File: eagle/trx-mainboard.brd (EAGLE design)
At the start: 95.3 x 82.5 mm, 38 parts, among them J1 629722000214, J2 DF12NB(3.0)-10DP-0.5V, P1 S2B-PH-SM4-TB, Q1 BSS84, U2 BQ2407X

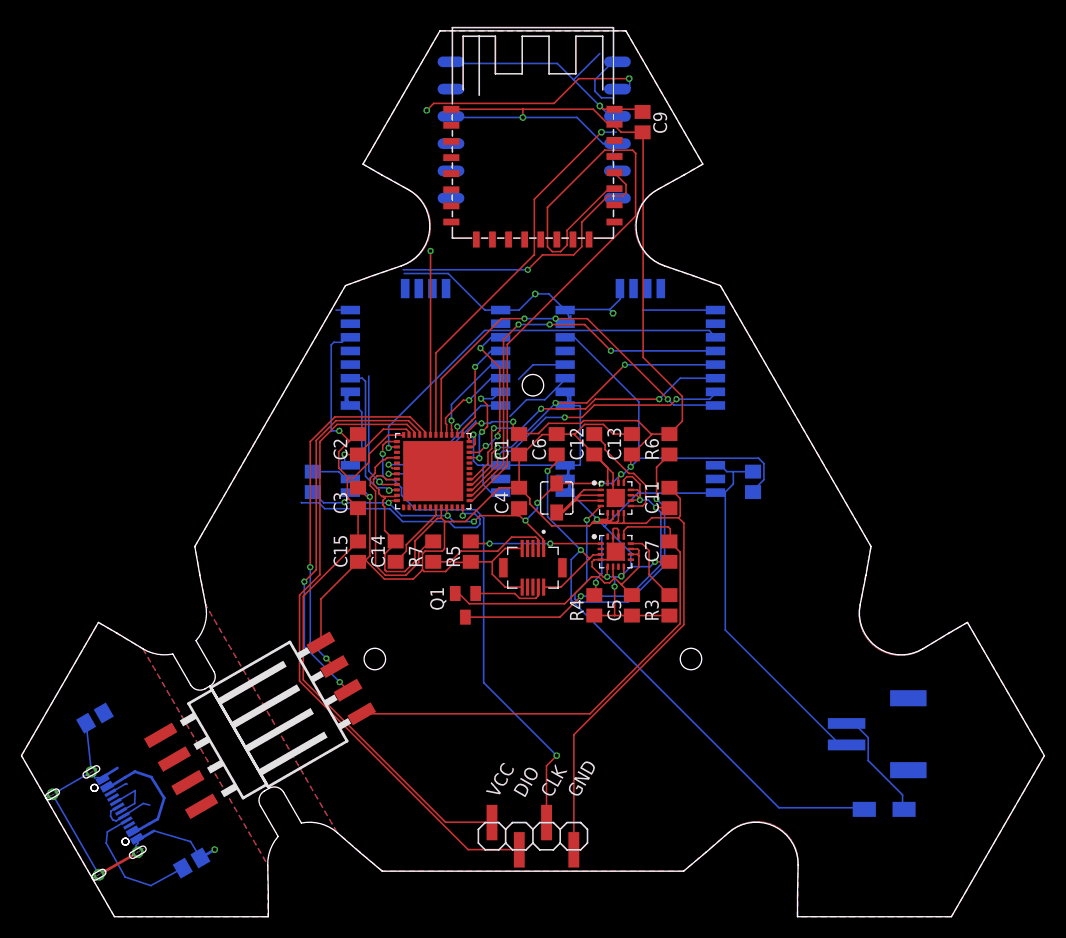
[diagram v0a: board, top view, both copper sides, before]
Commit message: Designed new boards wit fixed errors
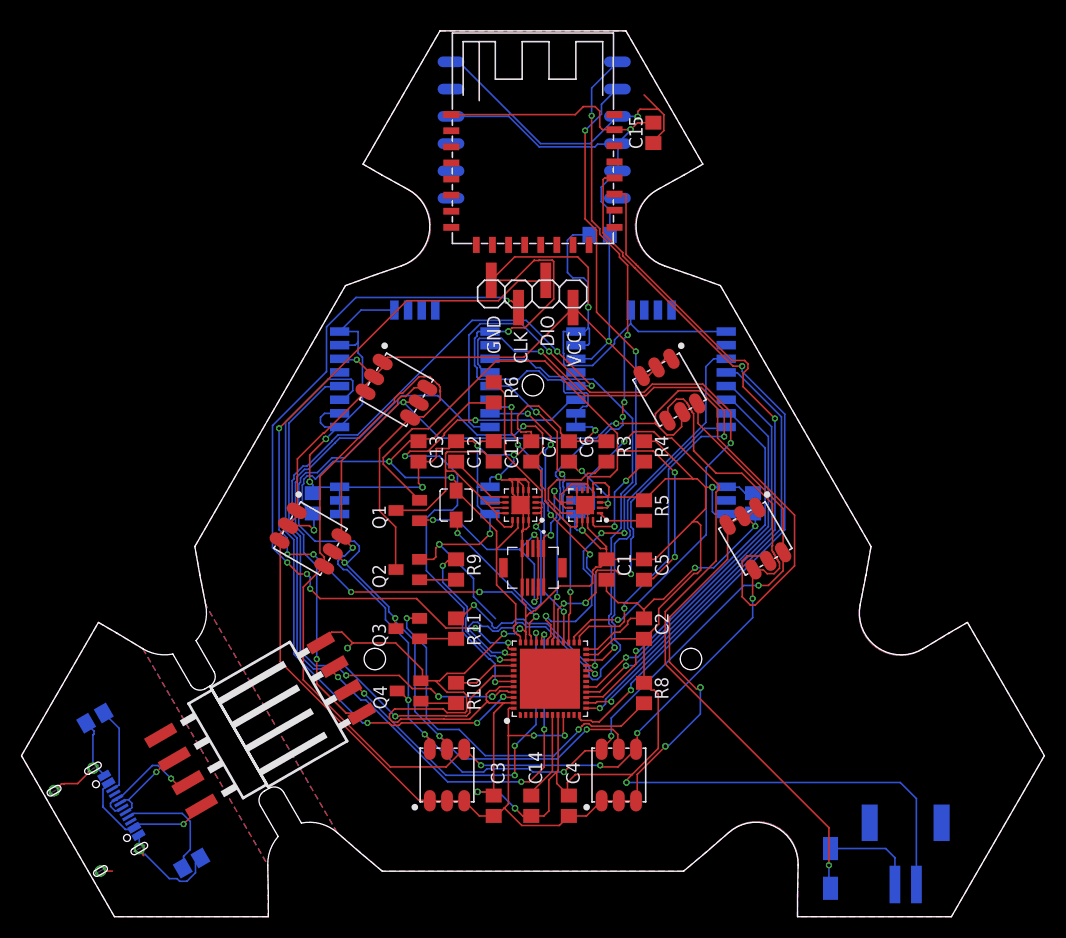
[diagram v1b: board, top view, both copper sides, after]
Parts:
- removed R7: 33R, rcl:R0805
- added Q2, Q3, Q4: BSS123, transistor-small-signal:SOT23
- added R10, R11, R8, R9: (no value), rcl:R0805
- added U$12, U$13, U$6, U$7, U$8, U$9: RGB_LED, led:PLCC6
- moved JP1 50.7 mm to (51.3, 59.0), turned to 180 degrees
- moved C15 47.7 mm to (60.0, 74.0)
- moved C2 31.7 mm to (59.1, 27.8)
- moved C3 31.3 mm to (45.1, 11.3)
- moved C4 29.0 mm to (52.1, 11.3)
- moved C14 26.8 mm to (48.6, 11.3), turned to 90 degrees
- moved U$10 22.2 mm to (50.4, 23.2)
- moved C13 19.9 mm to (38.1, 44.3), turned to 270 degrees
- moved R6 17.1 mm to (45.1, 49.8), turned to 90 degrees
- moved C11 16.9 mm to (45.1, 44.3)
- moved R5 16.6 mm to (59.1, 38.8), turned to 90 degrees
- moved C7 15.9 mm to (48.6, 44.3), turned to 90 degrees
- moved R3 15.5 mm to (55.6, 44.3), turned to 270 degrees
- moved R4 15.1 mm to (59.1, 44.3), turned to 270 degrees
- moved P1 15.0 mm to (83.5, 4.00), turned to 0 degrees
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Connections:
- removed net LED_D: J2.3, R7.1
- removed net N$10: R7.2, U$10.40
- removed net N$9: C5.1, Q1.2, U2.10, U2.11, U2.6
- new net CAT_B: Q4.3, U$12.2, U$13.2, U$6.2, U$7.2, U$8.2, U$9.2
- new net CAT_G: Q2.3, U$12.6, U$13.6, U$6.6, U$7.6, U$8.6, U$9.6
- new net CAT_R: Q3.3, U$12.4, U$13.4, U$6.4, U$7.4, U$8.4, U$9.4
- new net LED_B: R10.2, U$10.40
- new net LED_G: R9.2, U$10.39
- new net LED_R: R11.2, U$10.20
- new net N$13: Q2.1, R9.1
- new net N$14: Q3.2, R8.2
- new net N$16: Q4.1, R10.1
- new net N$18: Q3.1, R11.1
- new net VOUT: C5.1, J2.1, J2.2, Q1.2, U2.10, U2.11, U2.6
- net +3V3: now also U$12.1, U$12.3, U$12.5, U$13.1, U$13.3, U$13.5, U$6.1, U$6.3, U$6.5, U$7.1, U$7.3, U$7.5, U$8.1, U$8.3, U$8.5, U$9.1, U$9.3, U$9.5; no longer J2.1
- net GND: now also Q2.2, Q4.2, R8.1
- net PWR_TRIG: now also J2.3
- net USB_D+: now also U$3.2; no longer U$3.3
- net USB_D-: now also U$3.3; no longer U$3.2
- net VBAT+: no longer J2.2
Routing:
- net CAT_G: track 0.00 -> 140.7 mm, vias 0 -> 4
- net CAT_R: track 0.00 -> 140.0 mm, vias 0 -> 6
- net GND: track 376.0 -> 503.7 mm, vias 11 -> 20
- net CAT_B: track 0.00 -> 107.2 mm, vias 0 -> 6
- net VOUT: track 0.00 -> 75.9 mm, vias 0 -> 4
- net +3V3: track 235.9 -> 311.6 mm, vias 13 -> 12
- net LORA1_TXEN: track 15.4 -> 79.2 mm, vias 1 -> 3
- net LORA2_SSEL: track 5.62 -> 68.2 mm, vias 1 -> 3
- net LORA2_RST: track 9.81 -> 60.3 mm, vias 1 -> 3
- net LORA2_RXEN: track 13.9 -> 56.7 mm, vias 1 -> 3
- net LORA2_TXEN: track 12.6 -> 50.0 mm, vias 1 -> 3
- net N$14: track 0.00 -> 35.3 mm, vias 0 -> 2
- net LORA1_RXEN: track 17.7 -> 49.9 mm, vias 1 -> 3
- net LORA2_D0: track 14.6 -> 41.2 mm, vias 3 -> 1
- net N$9: track 25.6 -> 0.00 mm
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
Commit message: Modified board layout
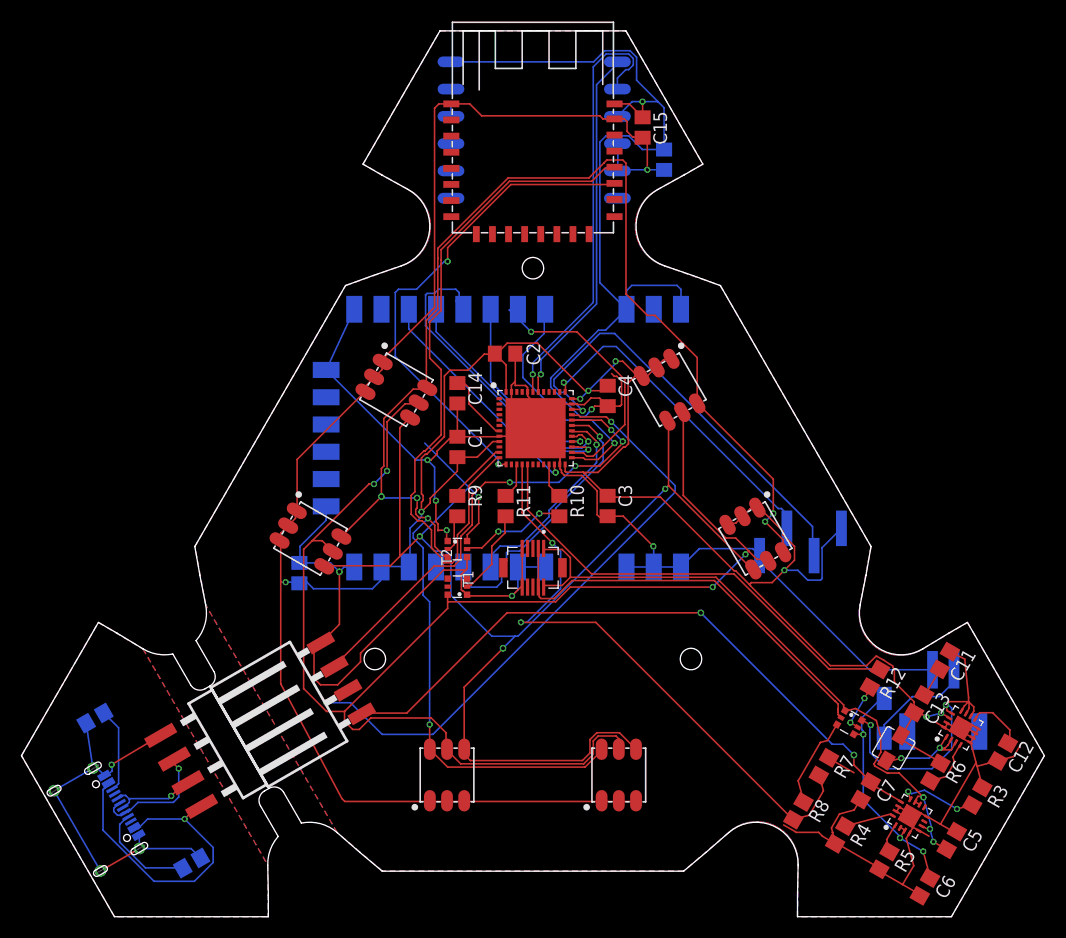
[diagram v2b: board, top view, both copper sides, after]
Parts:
- removed C8: 4.7uF, rcl:C0805
- removed LORA1, LORA2: E32-X00M20S, ebyte:E32-X00M20S
- removed Q1: BSS84, transistor-small-signal:SOT23
- removed Q2, Q3, Q4: BSS123, transistor-small-signal:SOT23
- added R12: 100R, rcl:R0805
- added R7: 10k, rcl:R0805
- added T1, T2: NX3008NBKS, NXP_60_26022015:SOT363
- added T3: NX3008PBKS, NXP_60_26022015:SOT363
- added U$14: E32-900M30S, ebyte:E32-900M30S
- R10, R11, R9: value (none) -> 100R
- R8: value (none) -> 10k
- U$10: value STM32-F042X4/6-48 -> STM32-F072X8/B-48
- moved C12 58.1 mm to (92.5, 16.3), turned to 240 degrees
- moved R6 54.2 mm to (86.3, 14.5), turned to 240 degrees
- moved C6 52.4 mm to (85.3, 3.78), turned to 240 degrees
- moved C13 52.2 mm to (84.8, 20.8), turned to 60 degrees
- moved R3 47.2 mm to (90.2, 12.2), turned to 240 degrees
- moved U$4 46.6 mm to (82.4, 16.7), turned to 60 degrees
- moved C11 46.3 mm to (87.1, 24.9), turned to 240 degrees
- moved U$2 46.0 mm to (88.6, 18.6), turned to 60 degrees
- moved C7 44.4 mm to (79.8, 12.7), turned to 240 degrees
- moved C10 42.7 mm to (27.0, 33.0)
- moved U2 41.9 mm to (83.9, 10.4), turned to 60 degrees
- moved R4 40.1 mm to (77.4, 8.62), turned to 60 degrees
- moved R5 39.5 mm to (81.5, 6.24), turned to 240 degrees
- moved C14 39.0 mm to (41.8, 49.8)
- moved C4 38.3 mm to (55.8, 49.5), turned to 270 degrees
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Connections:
- removed net LORA1_D0: LORA1.18, U$10.38
- removed net LORA1_MISO: LORA1.20, U$10.16
- removed net LORA1_MOSI: LORA1.21, U$10.17
- removed net LORA1_RST: LORA1.19, U$10.14
- removed net LORA1_RXEN: LORA1.6, U$10.43
- removed net LORA1_SCK: LORA1.22, U$10.15
- removed net LORA1_SSEL: LORA1.23, U$10.29
- removed net LORA1_TXEN: LORA1.7, U$10.42
- new net N$17: R12.1, T3.5
- new net VBAT_EN: R12.2, U$10.17
- new net VBAT_REF: R7.1, R8.2, U$10.16
- net +3V3: now also U$14.10, U$14.9; no longer C8.1, LORA1.9, LORA2.9
- net CAT_B: now also T1.3; no longer Q4.3
- net CAT_G: now also T1.6; no longer Q2.3
- net CAT_R: now also T2.6; no longer Q3.3
- net GND: now also R7.2, T1.1, T1.4, T2.1, U$10.P$49, U$14.1, U$14.11, U$14.12, U$14.17, U$14.18, U$14.2, U$14.26, U$14.28, U$14.3, U$14.4, U$14.5; no longer C8.2, LORA1.1, LORA1.10, LORA1.11, LORA1.12, LORA1.16, LORA1.2, LORA1.24, LORA1.26, LORA1.3, LORA1.4, LORA1.5, LORA2.1, LORA2.10, LORA2.11, LORA2.12, LORA2.16, LORA2.2, LORA2.24, LORA2.26, LORA2.3, LORA2.4, LORA2.5, Q2.2, Q4.2, R8.1
- net GPS_RX: now also U$10.42; no longer U$10.30
- net GPS_TX: now also U$10.43; no longer U$10.31
- net LED_B: now also U$10.21; no longer U$10.40
- net LED_G: now also U$10.11; no longer U$10.39
- net LED_R: now also U$10.15; no longer U$10.20
- net LORA2_D0: now also U$14.20; no longer LORA2.18
- net LORA2_MISO: now also U$14.22; no longer LORA2.20
- net LORA2_MOSI: now also U$14.23; no longer LORA2.21
- net LORA2_RST: now also U$10.29, U$14.21; no longer LORA2.19, U$10.25
- net LORA2_RXEN: now also U$10.30, U$14.6; no longer LORA2.6, U$10.46
- net LORA2_SCK: now also U$10.26, U$14.24; no longer LORA2.22, U$10.21
- net LORA2_SSEL: now also U$10.25, U$14.25; no longer LORA2.23, U$10.26
- net LORA2_TXEN: now also U$10.31, U$14.7; no longer LORA2.7, U$10.45
- net N$13: now also T1.2; no longer Q2.1
- net N$14: now also R8.1, T3.3; no longer Q3.2, R8.2
- net N$16: now also T1.5; no longer Q4.1
- net N$18: now also T2.2; no longer Q3.1
- net PWR_TRIG: now also T3.2; no longer Q1.1
- net V+: now also T3.6; no longer Q1.3
- net VBAT+: now also T3.4
- net VOUT: now also T3.1; no longer Q1.2
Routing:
- net GND: track 503.7 -> 354.0 mm, vias 20 -> 8
- net LORA1_TXEN: track 79.2 -> 0.00 mm, vias 3 -> 0
- net LORA1_D0: track 57.5 -> 0.00 mm, vias 1 -> 0
- net VBAT_REF: track 0.00 -> 56.8 mm, vias 0 -> 2
- net LORA1_RXEN: track 49.9 -> 0.00 mm, vias 3 -> 0
- net VBAT+: track 69.6 -> 23.1 mm, vias 4 -> 3
- net LORA2_SSEL: track 68.2 -> 23.0 mm, vias 3 -> 1
- net VBAT_EN: track 0.00 -> 43.3 mm
- net LORA1_RST: track 42.3 -> 0.00 mm, vias 1 -> 0
- net CAT_B: track 107.2 -> 147.2 mm
- net LORA1_MISO: track 38.8 -> 0.00 mm, vias 1 -> 0
- net SWCLK: track 69.3 -> 31.0 mm, vias 6 -> 1
- net LORA2_RST: track 60.3 -> 22.9 mm, vias 3 -> 1
- net LORA1_MOSI: track 36.9 -> 0.00 mm, vias 1 -> 0
- net LORA2_RXEN: track 56.7 -> 19.9 mm, vias 3 -> 1
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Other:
- board text removed: "LORA2"
